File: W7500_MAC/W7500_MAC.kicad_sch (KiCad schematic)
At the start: 0 parts

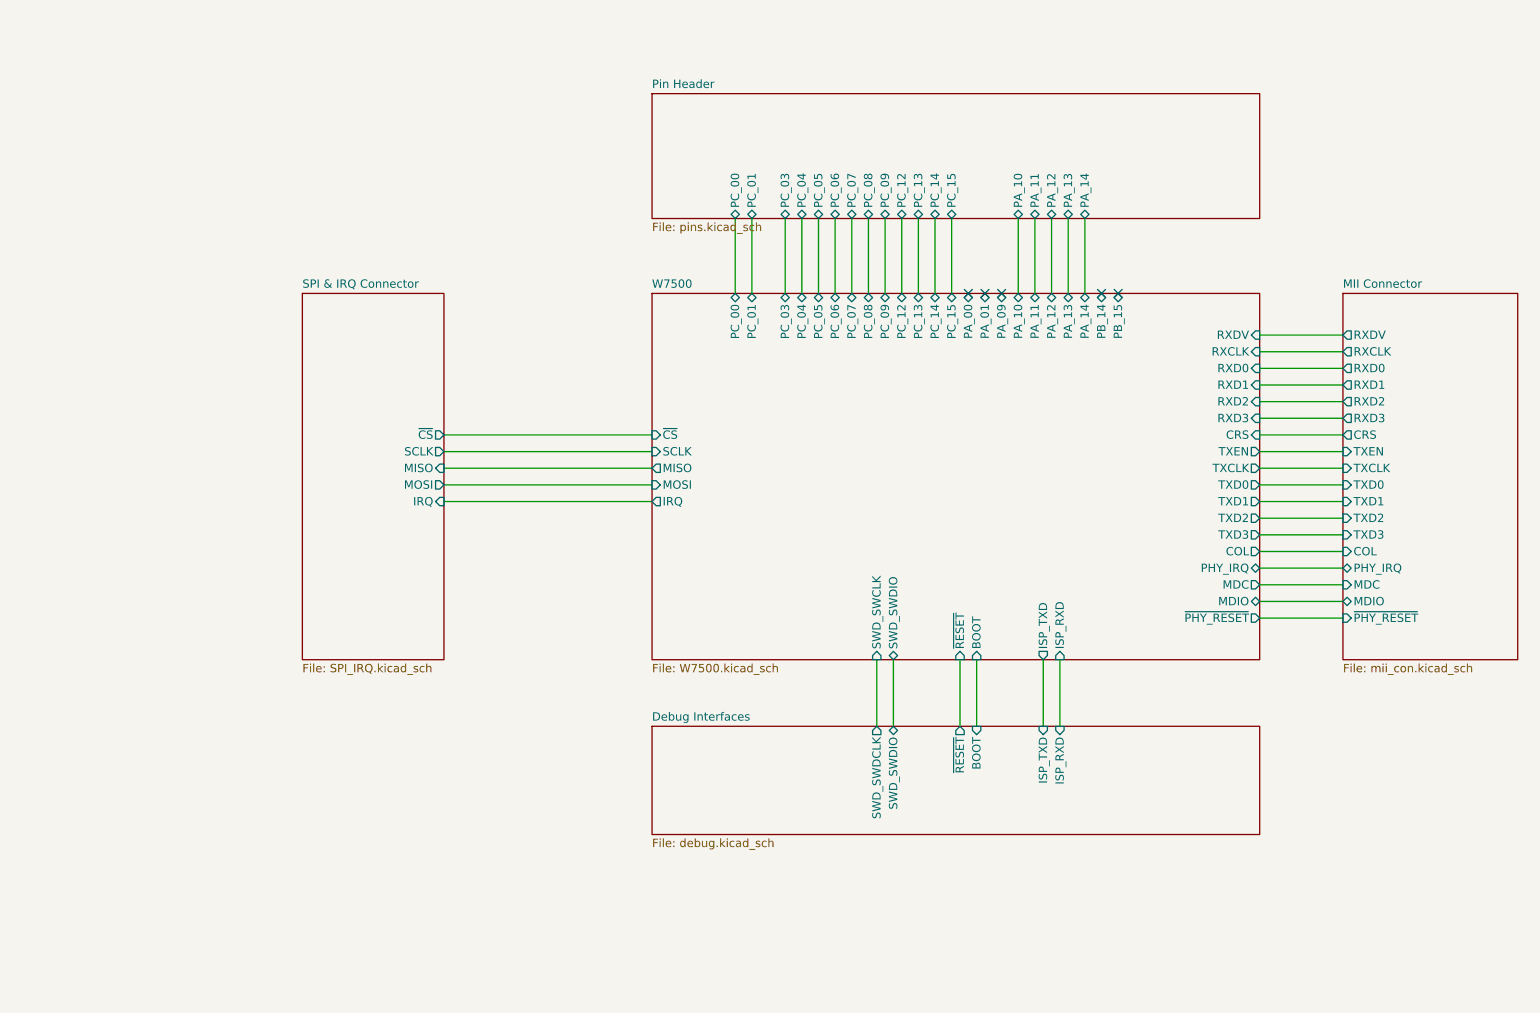
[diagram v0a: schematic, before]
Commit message: W7500 MAC redesign to manufactured version
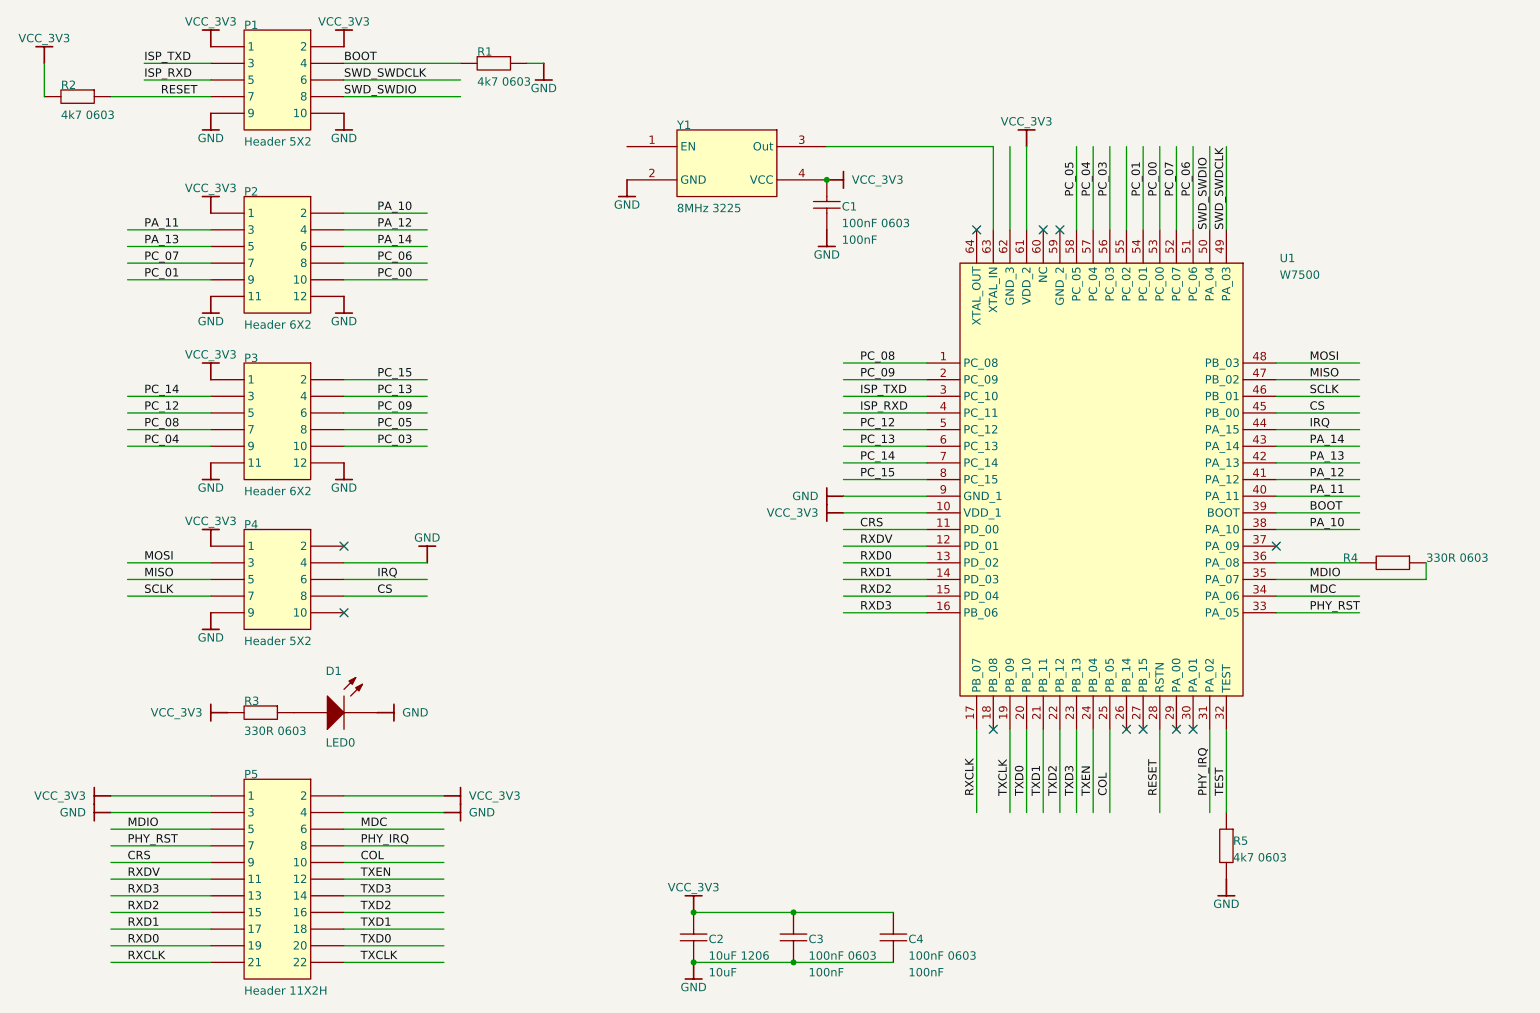
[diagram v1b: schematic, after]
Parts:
- added C1, C3, C4: 100nF 0603, 0603_CAP, symbol Miscellaneous Devices:root_1_Cap_Miscellaneous Devices.IntLib
- added C2: 10uF 1206, 1206_CAP, symbol Miscellaneous Devices:root_1_Cap_Miscellaneous Devices.IntLib
- added D1: LED0, 0603_LED, symbol Miscellaneous Devices:root_0_LED0_Miscellaneous Devices.IntLib
- added P1, P4: Header 5X2, HDR2X5, symbol Miscellaneous Connectors:root_0_Header 5X2_Miscellaneous Connectors.IntLib
- added P2, P3: Header 6X2, HDR2X6, symbol Miscellaneous Connectors:root_0_Header 6X2_Miscellaneous Connectors.IntLib
- added P5: Header 11X2H, HDR2X11, symbol Miscellaneous Connectors:root_0_Header 11X2H_Miscellaneous Connectors.IntLib
- added R1, R2: 4k7 0603, 0603, symbol Miscellaneous Devices:root_0_mirrored_Res2_Miscellaneous Devices.IntLib
- added R3, R4: 330R 0603, 0603, symbol Miscellaneous Devices:root_0_mirrored_Res2_Miscellaneous Devices.IntLib
- added R5: 4k7 0603, 0603, symbol Miscellaneous Devices:root_1_mirrored_Res2_Miscellaneous Devices.IntLib
- added U1: W7500, W7500_64pin, symbol pcSwitchLib:root_0_W7500_pcSwitchLib.SchLib
- added Y1: 8MHz 3225, XTAL_3225, symbol pcSwitchLib:root_0_XTAL_pcSwitchLib.SchLib
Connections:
- new net: D1.1 (A), R3.1
- new net: R4.2, U1.36 (PA_08)
- new net: U1.63 (XTAL_IN), Y1.3 (Out)
- new net BOOT: P1.4, R1.2, U1.39 (BOOT)
- new net COL: P5.10, U1.25 (PB_05)
- new net CRS: P5.9, U1.11 (PD_00)
- new net CS: P4.8, U1.45 (PB_00)
- new net GND: C1.1, C2.1, C3.1, C4.1, D1.2 (K), P1.10, P1.9, P2.11, P2.12, P3.11, P3.12, P4.4, P4.9, P5.3, P5.4, R1.1, R5.1, U1.9 (GND_1), Y1.2 (GND)
- new net IRQ: P4.6, U1.44 (PA_15)
- new net ISP_RXD: P1.5, U1.4 (PC_11)
- new net ISP_TXD: P1.3, U1.3 (PC_10)
- new net MDC: P5.6, U1.34 (PA_06)
- new net MDIO: P5.5, R4.1, U1.35 (PA_07)
- new net MISO: P4.5, U1.47 (PB_02)
- new net MOSI: P4.3, U1.48 (PB_03)
- new net PA_10: P2.2, U1.38 (PA_10)
- new net PA_11: P2.3, U1.40 (PA_11)
- new net PA_12: P2.4, U1.41 (PA_12)
- new net PA_13: P2.5, U1.42 (PA_13)
- new net PA_14: P2.6, U1.43 (PA_14)
- new net PC_00: P2.10, U1.53 (PC_00)
- new net PC_01: P2.9, U1.54 (PC_01)
- new net PC_03: P3.10, U1.56 (PC_03)
- new net PC_04: P3.9, U1.57 (PC_04)
- new net PC_05: P3.8, U1.58 (PC_05)
- new net PC_06: P2.8, U1.51 (PC_06)
- new net PC_07: P2.7, U1.52 (PC_07)
- new net PC_08: P3.7, U1.1 (PC_08)
- new net PC_09: P3.6, U1.2 (PC_09)
- new net PC_12: P3.5, U1.5 (PC_12)
- new net PC_13: P3.4, U1.6 (PC_13)
- new net PC_14: P3.3, U1.7 (PC_14)
- new net PC_15: P3.2, U1.8 (PC_15)
- new net PHY_IRQ: P5.8, U1.31 (PA_02)
- new net PHY_RST: P5.7, U1.33 (PA_05)
- new net RESET: P1.7, R2.1, U1.28 (RSTN)
- new net RXCLK: P5.21, U1.17 (PB_07)
- new net RXD0: P5.19, U1.13 (PD_02)
- new net RXD1: P5.17, U1.14 (PD_03)
- new net RXD2: P5.15, U1.15 (PD_04)
- new net RXD3: P5.13, U1.16 (PB_06)
- new net RXDV: P5.11, U1.12 (PD_01)
- new net SCLK: P4.7, U1.46 (PB_01)
- new net SWD_SWDCLK: P1.6, U1.49 (PA_03)
- new net SWD_SWDIO: P1.8, U1.50 (PA_04)
- new net TEST: R5.2, U1.32 (TEST)
- new net TXCLK: P5.22, U1.19 (PB_09)
- new net TXD0: P5.20, U1.20 (PB_10)
- new net TXD1: P5.18, U1.21 (PB_11)
- new net TXD2: P5.16, U1.22 (PB_12)
- new net TXD3: P5.14, U1.23 (PB_13)
- new net TXEN: P5.12, U1.24 (PB_04)
- new net VCC_3V3: C1.2, C2.2, C3.2, C4.2, P1.1, P1.2, P2.1, P3.1, P4.1, P5.1, P5.2, R2.2, R3.2, U1.10 (VDD_1), U1.61 (VDD_2), Y1.4 (VCC)
- no-connect marks 5 -> 11
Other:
- removed sheet Debug Interfaces
- removed sheet MII Connector
- removed sheet Pin Header
- removed sheet SPI & IRQ Connector
- removed sheet W7500
- title: W7500 MAC Card -> (none)
